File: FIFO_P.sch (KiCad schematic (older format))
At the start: 93 parts, among them J1 Vin, J2 ICLK, J3 Screw_Terminal_01x08, J4 Jack-DC, J5 Start Trigger, J6 Vout, SW1 Program History, SW2 Rotary_Encoder_61C, U1 IDT_ICS551, U10 AD7840, U11 LM2776, U2 SN74LVC2G157_MUX_TI, U3 SN74LVC2G157_MUX_TI, U4 LTC1740, U5 LM2940CT-5.0, U6 LM1117-3.3, U7 ARDUINO_DUE_FIFO_P_COMMANDS, U8 IDT_72V2105, U9 Adafruit_128x32_OLED_I2C_1306

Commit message: Calculated optimum DAC0 to ADC resistor values and fixed schematic
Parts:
- removed R?: 30R1, symbol Device:R
- removed R?: 10k, symbol Device:R
- removed R?: 220R, symbol Device:R
- added R?: 30R1, symbol Device:R
- R?: value 220R -> 1k1
- R? (x3): value 10k -> 5k1
- R?: value 10k -> 4k3
- R?: value 10k -> 1k1
- R?: value 10k -> 3k9
- RV?: value 5k -> 1k
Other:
- moved on the sheet: C?, R?, RV?, U?, U?A, U?B, U?C

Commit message: Updated schematic for dual clock operation; Squished everything!
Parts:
- removed C11: 1u, Capacitor_SMD:C_0805_2012Metric_Pad1.15x1.40mm_HandSolder, symbol Device:C
- removed C8: 0u1, Capacitor_SMD:C_0805_2012Metric_Pad1.15x1.40mm_HandSolder, symbol Device:C
- removed J2: ICLK, Connector_Coaxial:BNC_TEConnectivity_1478204_Vertical, symbol Connector:Conn_Coaxial
- removed R2: 49R9, Resistor_SMD:R_0805_2012Metric_Pad1.15x1.40mm_HandSolder, symbol Device:R
- removed SW1: Program History, Button_Switch_THT:SW_Slide_1P2T_CK_OS102011MS2Q, symbol Switch:SW_SPDT
- removed TP2: TestPoint, FIFO_P:Test_Pin, symbol Connector:TestPoint
- removed U1: IDT_ICS551, Package_SO:SOIC-8_3.9x4.9mm_P1.27mm, symbol FIFO_P:IDT_ICS551
- added C12: 1u, Capacitor_SMD:C_0805_2012Metric_Pad1.15x1.40mm_HandSolder, symbol Device:C
- added C20, C21, C9: 0u1, Capacitor_SMD:C_0805_2012Metric_Pad1.15x1.40mm_HandSolder, symbol Device:C
- added C42, C43: 10u, Capacitor_SMD:C_0805_2012Metric_Pad1.15x1.40mm_HandSolder, symbol Device:C
- added J4: XWCLK, Connector_Coaxial:BNC_TEConnectivity_1478204_Vertical, symbol Connector:Conn_Coaxial
- added J5: XRCLK, Connector_Coaxial:BNC_TEConnectivity_1478204_Vertical, symbol Connector:Conn_Coaxial
- added R7, R8: 49R9, Resistor_SMD:R_0805_2012Metric_Pad1.15x1.40mm_HandSolder, symbol Device:R
- added U2: SN74LVC2G157_MUX_TI, Package_SO:SSOP-8_2.95x2.8mm_P0.65mm, symbol FIFO_P:SN74LVC2G157_MUX_TI
- added U3: TS12A12511, Package_TO_SOT_SMD:SOT-23-8_Handsoldering, symbol FIFO_P:TS12A12511
- C13, C44: renamed from C?; footprint (none) -> Capacitor_SMD:C_0805_2012Metric_Pad1.15x1.40mm_HandSolder
- R10: renamed from R7; footprint Resistor_THT:R_Axial_DIN0207_L6.3mm_D2.5mm_P10.16mm_Horizontal -> Resistor_SMD:R_0805_2012Metric_Pad1.15x1.40mm_HandSolder
- R11, R14, R15, R16, R17, R18, R5, R9: renamed from R?; footprint (none) -> Resistor_SMD:R_0805_2012Metric_Pad1.15x1.40mm_HandSolder
- R12: renamed from R8; footprint Resistor_THT:R_Axial_DIN0207_L6.3mm_D2.5mm_P10.16mm_Horizontal -> Resistor_SMD:R_0805_2012Metric_Pad1.15x1.40mm_HandSolder
- R13: renamed from R9; footprint Resistor_THT:R_Axial_DIN0207_L6.3mm_D2.5mm_P10.16mm_Horizontal -> Resistor_SMD:R_0805_2012Metric_Pad1.15x1.40mm_HandSolder
- R3: value 30R1 -> 22R6
- R6: footprint Resistor_THT:R_Axial_DIN0204_L3.6mm_D1.6mm_P7.62mm_Horizontal -> Resistor_SMD:R_0805_2012Metric_Pad1.15x1.40mm_HandSolder
- RV1, RV3: renamed from RV?; footprint (none) -> Potentiometer_SMD:Potentiometer_Vishay_TS53YL_Vertical
- SW1: renamed from SW2; footprint Connector_PinHeader_2.54mm:PinHeader_1x06_P2.54mm_Vertical -> FIFO_P:Rotary_Encoder_61C
- U10: renamed from U9; footprint Connector_PinHeader_2.54mm:PinHeader_1x06_P2.54mm_Vertical -> FIFO_P:Adafruit_128x32_OLED_I2C_1306
- U12: renamed from U?; footprint Package_TO_SOT_THT:TO-92_Inline -> Package_TO_SOT_SMD:SOT-23_Handsoldering
- U14: renamed from U?; footprint (none) -> Package_SO:SOIC-8_3.9x4.9mm_P1.27mm
- renumbered C12 to C11, C13 to C14, C14 to C15, C15 to C16, C16 to C17, C17 to C18, C18 to C19, C19 to C22, C20 to C23, C21 to C24, C22 to C25, C23 to C26, C24 to C27, C25 to C28, C26 to C29, C27 to C30, C28 to C31, C29 to C32, C30 to C33, C31 to C34, C32 to C35, C33 to C36, C36 to C37, C34 to C38, C35 to C39, C37 to C40, C38 to C41, C9 to C8, J3 to J2, J4 to J3, J5 to J6, J6 to J7, R4 to R2, R5 to R4, RV1 to RV2, TP3 to TP2, TP4 to TP3, TP5 to TP4, TP6 to TP5, TP7 to TP6, U2 to U1, U10 to U11, U11 to U13, U3 to U4, U4 to U5, U5 to U6, U6 to U7, U7 to U8, U8 to U9
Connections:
- net labels added: ADC_CLK_S, PROG_D, RHALT
- net labels removed: DAC_WR, WLSTN
- wire segments 443 -> 456
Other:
- note added: "TS12A12511 Decoupling"
- note removed: "Analog star\nGND"
- moved on the sheet: C10, C11, C13, C14, C33, C34, C35, C36, C37, C38, C39, C40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

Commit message: Fixed Due power and added AND gate for FIFO ~RE
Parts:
- added U11: 74AHC1G08, Package_SO:TSOP-5_1.65x3.05mm_P0.95mm, symbol 74xGxx:74AHC1G08
- renumbered R9 to R10, R12 to R11, R13 to R12, R11 to R13, R10 to R9, U11 to U12, U12 to U13, U13 to U14, U14 to U15
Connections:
- net labels added: A1, A2, RST1
- wire segments 456 -> 459
- no-connect marks 12 -> 9
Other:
- moved on the sheet: U10

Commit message: Almost done routing!
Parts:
- removed R2, R3, R4: 22R6, Resistor_SMD:R_0805_2012Metric_Pad1.15x1.40mm_HandSolder, symbol Device:R
- renumbered C14 to C13, C15 to C14, C16 to C15, C17 to C16, C18 to C17, C19 to C18, C20 to C19, C21 to C20, C22 to C21, C23 to C22, C24 to C23, C25 to C24, C26 to C25, C27 to C26, C28 to C27, C29 to C28, C30 to C29, C31 to C30, C32 to C31, C13 to C32, R13 to R10, R14 to R11, R15 to R12, R16 to R13, R17 to R14, R18 to R15, R6 to R2, R7 to R3, R8 to R4, R9 to R6, R10 to R7, R11 to R8, R12 to R9, U3 to U1, U1 to U2, U2 to U3
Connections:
- net labels added: ~PROG
- wire segments 459 -> 458
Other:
- note added: "MUX out Z: about 22R6"
- moved on the sheet: C32, R5, U1

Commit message: Done with main circuit. TODO: EXT header and input protection
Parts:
- removed TP1, TP2, TP3, TP4, TP5, TP6: TestPoint, FIFO_P:Test_Pin, symbol Connector:TestPoint
- added J6: Conn_02x04_Odd_Even, Connector_PinSocket_2.54mm:PinSocket_2x04_P2.54mm_Vertical, symbol Connector_Generic:Conn_02x04_Odd_Even
- added R2: 22R, Resistor_SMD:R_0805_2012Metric_Pad1.15x1.40mm_HandSolder, symbol Device:R
- R10: renamed from R9; value 10k -> 5k1
- R6: renamed from R5; value 30R1 -> 22R
- R7: renamed from R6; value 3k3 -> 5k1
- R9: renamed from R8; value 3k3 -> 5k1
- renumbered J6 to J7, J7 to J8, R10 to R11, R11 to R12, R12 to R13, R13 to R14, R14 to R15, R15 to R16, R2 to R3, R3 to R4, R4 to R5, R7 to R8
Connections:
- net labels removed: CLK_EN, PROG, RCLK_S, RLSTN
- wire segments 458 -> 467
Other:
- note removed: "MUX out Z: about 22R6"
- moved on the sheet: J7

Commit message: Board pretty much done. Cleaned up silkscreen
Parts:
- added Q1: DMP3099L, Package_TO_SOT_SMD:SOT-23, symbol FIFO_P:DMP3099L
- added TP1: GND, FIFO_P:Test_Pin, symbol Connector:TestPoint_Alt
- added TP2: +5V, FIFO_P:Test_Pin, symbol Connector:TestPoint_Alt
- added TP3: -5V, FIFO_P:Test_Pin, symbol Connector:TestPoint_Alt
- added TP4: 3.3V, FIFO_P:Test_Pin, symbol Connector:TestPoint_Alt
- renumbered C17 to C16, C18 to C17, C19 to C18, C16 to C19, C23 to C22, C22 to C23, C6 to C5, C5 to C6, C8 to C7, C9 to C8, C7 to C9, J3 to J2, J2 to J3
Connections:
- net +5V: now also TP2.1
- net -5V: now also TP3.1
- net A1: now also U8.A1
- net A2: now also U8.A2
- net GND: now also Q1.1 (G), TP1.1
- net RST1: now also U8.RST1
- net V+: now also Q1.2 (S); no longer J2.1, J3.8 (Pin_8)
- net VCC: now also TP4.1
- net at U8.5V3 (EXT_5V): now also J6.2 (Pin_2)
- net at U8.D23: now also J6.6 (Pin_6); no longer J6.5 (Pin_5)
- net at U8.D25: now also J6.8 (Pin_8); no longer J6.7 (Pin_7)
- net at U8.D27: now also J6.7 (Pin_7); no longer J6.8 (Pin_8)
- net at U8.D29: now also J6.5 (Pin_5); no longer J6.6 (Pin_6)
- new net: J2.1, J3.8 (Pin_8), Q1.3 (D)
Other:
- note added: "Reverse\nVoltage\nProtection"
- moved on the sheet: C14, C15, C19, C23, C24, C25, C4, C6, C9, J2, J6, U6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

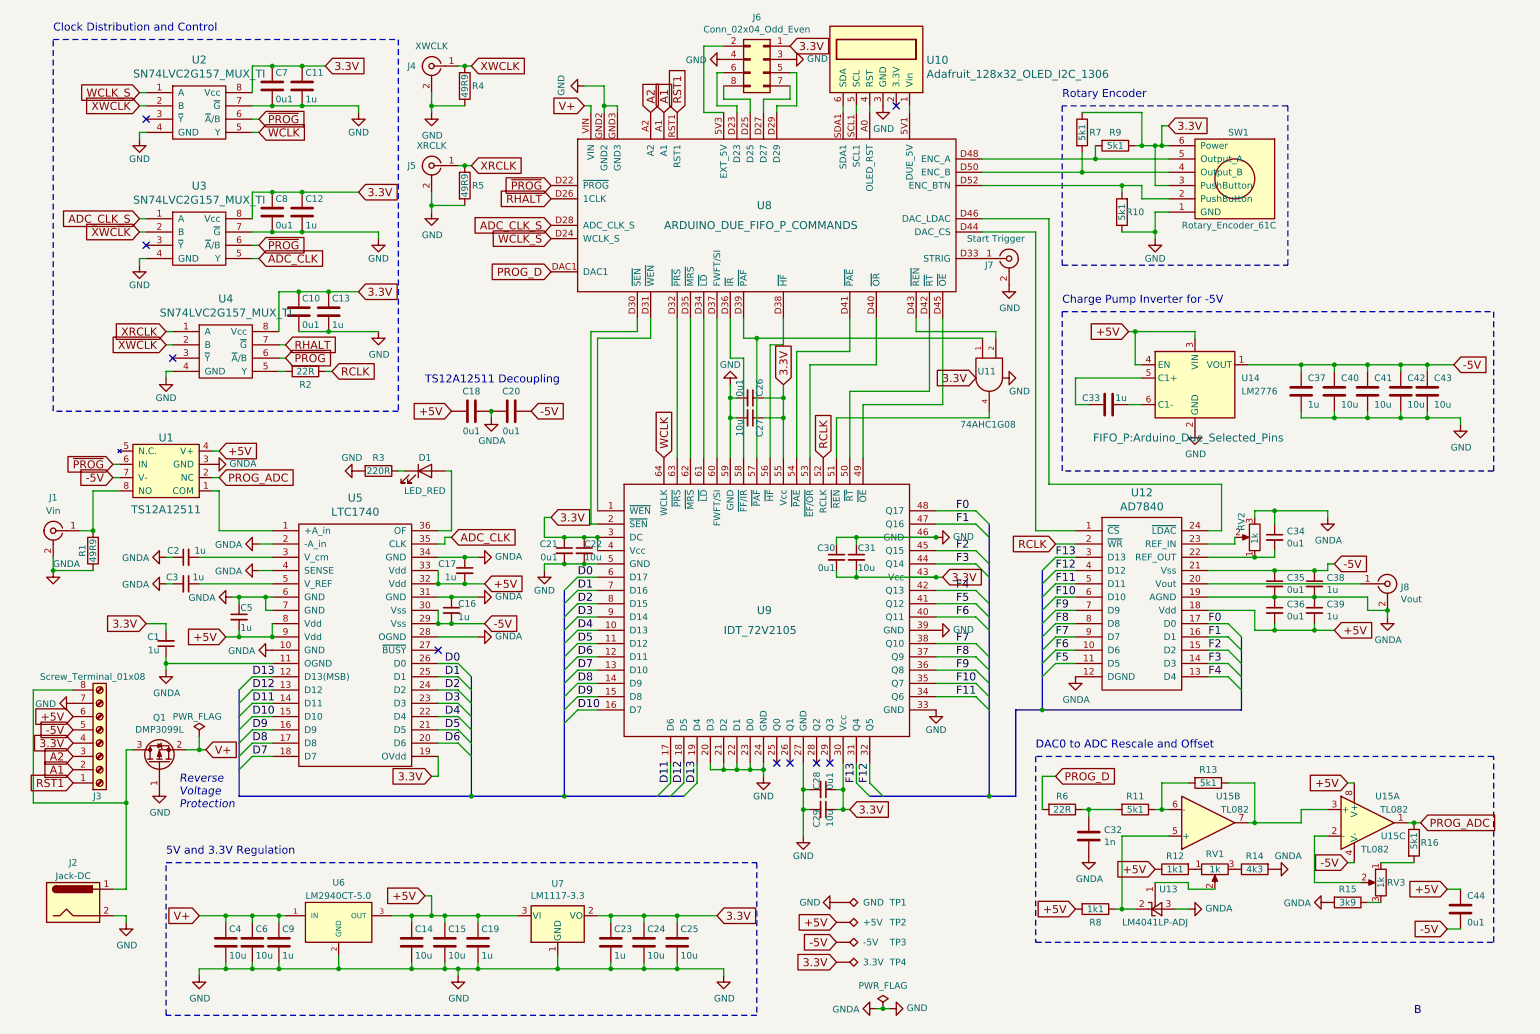
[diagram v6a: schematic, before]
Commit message: Fixed 1CLK signal. Board complete.
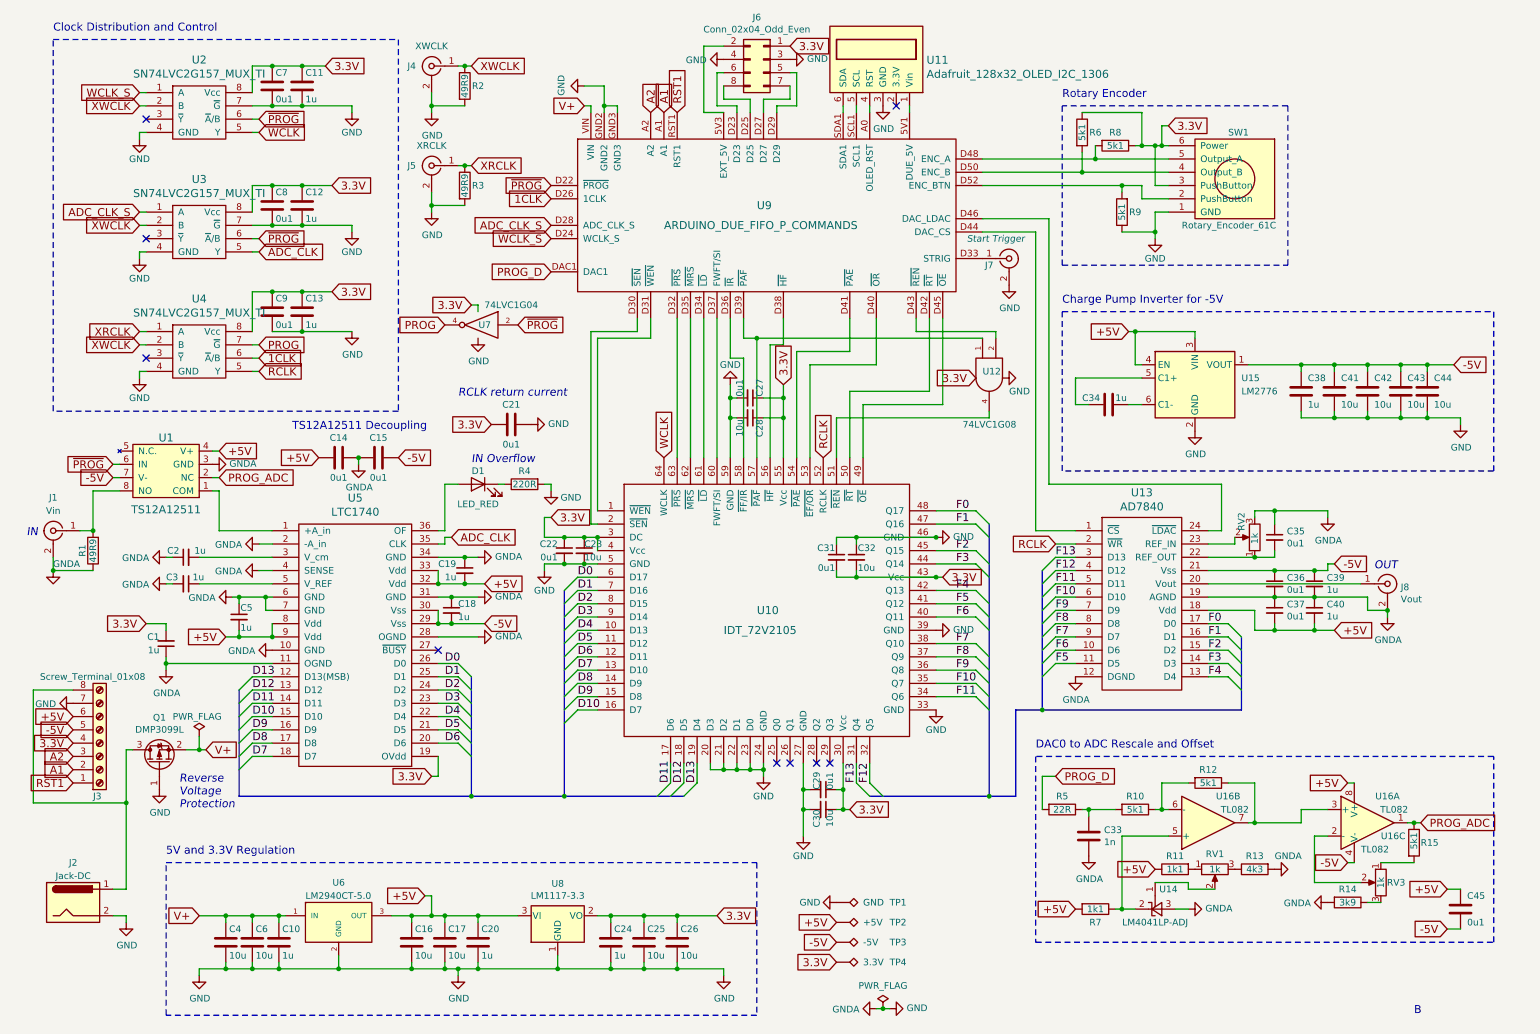
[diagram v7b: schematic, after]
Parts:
- removed R2: 22R, Resistor_SMD:R_0805_2012Metric_Pad1.15x1.40mm_HandSolder, symbol Device:R
- removed U11: 74AHC1G08, Package_SO:TSOP-5_1.65x3.05mm_P0.95mm, symbol 74xGxx:74AHC1G08
- added C21: 0u1, Capacitor_SMD:C_0805_2012Metric_Pad1.15x1.40mm_HandSolder, symbol Device:C
- added U12: 74LVC1G08, Package_TO_SOT_SMD:SOT-23-5_HandSoldering, symbol 74xGxx:74LVC1G08
- added U7: 74LVC1G04, Package_TO_SOT_SMD:SOT-23-5_HandSoldering, symbol 74xGxx:74LVC1G04
- renumbered C9 to C10, C18 to C14, C20 to C15, C14 to C16, C15 to C17, C16 to C18, C17 to C19, C19 to C20, C21 to C22, C22 to C23, C23 to C24, C24 to C25, C25 to C26, C26 to C27, C27 to C28, C28 to C29, C29 to C30, C30 to C31, C31 to C32, C32 to C33, C33 to C34, C34 to C35, C35 to C36, C36 to C37, C37 to C38, C38 to C39, C39 to C40, C40 to C41, C41 to C42, C42 to C43, C43 to C44, C44 to C45, C10 to C9, R11 to R10, R12 to R11, R13 to R12, R14 to R13, R15 to R14, R16 to R15, R4 to R2, R5 to R3, R3 to R4, R6 to R5, R7 to R6, R8 to R7, R9 to R8, R10 to R9, U9 to U10, U10 to U11, U12 to U13, U13 to U14, U14 to U15, U15 to U16, U7 to U8, U8 to U9
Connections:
- net GND: now also C21.2, U12.3 (GND), U7.3 (GND)
- net RCLK: now also U4.5 (Y)
- net VCC: now also C21.1, U12.5 (VCC), U7.5 (VCC)
- net ~PROG: now also U7.2; no longer U4.6 (~A~/B~)
- net at U10.51 (~REN): now also U12.4
- net at U10.57 (~PAF), U9.D39 (~PAF): now also U12.1
- net at U9.D43 (~REN): now also U12.2
- net RHALT renamed 1CLK
- net 1CLK: now also U4.6 (~A~/B~); no longer U4.7 (~G)
- new net PROG: U4.7 (~G), U7.4
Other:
- note added: "IN"
- note added: "IN Overflow"
- note added: "OUT"
- note added: "RCLK return current"
- moved on the sheet: C12, C13, C14, C15, C8, C9, D1, R4, U3, U4

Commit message: Moved power connector for new Due header clearance
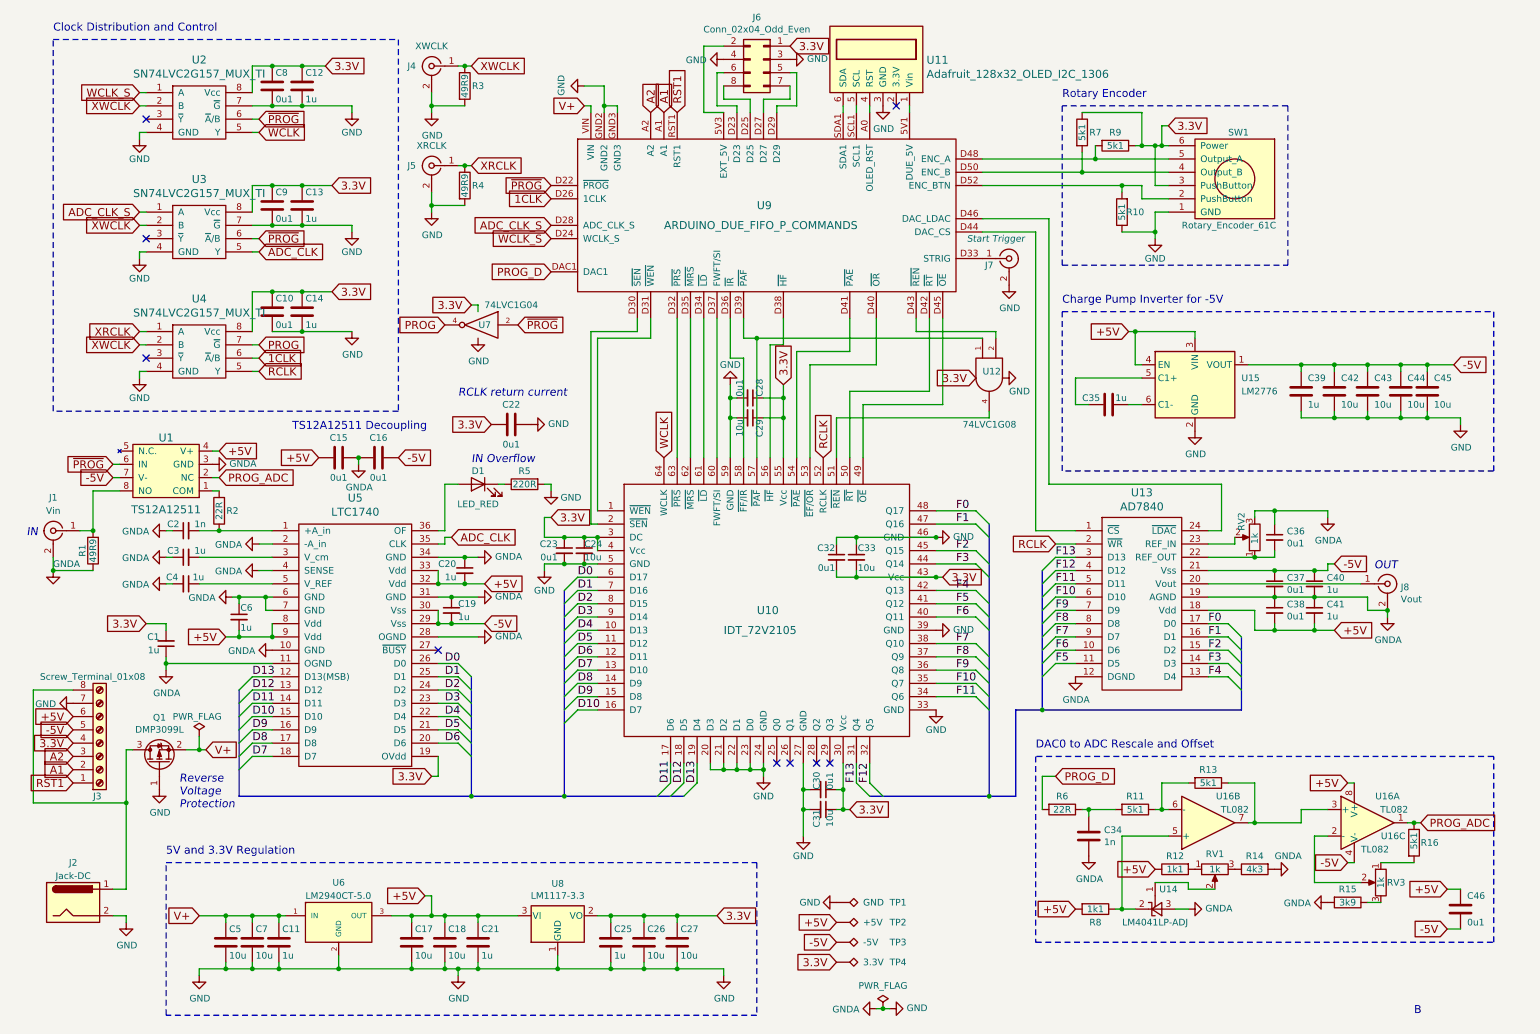
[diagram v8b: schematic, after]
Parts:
- added C2: 1n, Capacitor_SMD:C_0805_2012Metric_Pad1.15x1.40mm_HandSolder, symbol Device:C_Small
- added R2: 22R, Resistor_SMD:R_0805_2012Metric_Pad1.15x1.40mm_HandSolder, symbol Device:R
- renumbered C9 to C10, C10 to C11, C11 to C12, C12 to C13, C13 to C14, C14 to C15, C15 to C16, C16 to C17, C17 to C18, C18 to C19, C19 to C20, C20 to C21, C21 to C22, C22 to C23, C23 to C24, C24 to C25, C25 to C26, C26 to C27, C27 to C28, C28 to C29, C2 to C3, C29 to C30, C30 to C31, C31 to C32, C32 to C33, C33 to C34, C34 to C35, C35 to C36, C36 to C37, C37 to C38, C38 to C39, C3 to C4, C39 to C40, C40 to C41, C41 to C42, C42 to C43, C43 to C44, C44 to C45, C45 to C46, C4 to C5, C5 to C6, C6 to C7, C7 to C8, C8 to C9, R9 to R10, R10 to R11, R11 to R12, R12 to R13, R13 to R14, R14 to R15, R15 to R16, R2 to R3, R3 to R4, R4 to R5, R5 to R6, R6 to R7, R7 to R8, R8 to R9
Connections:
- net GND: now also C2.1
- net at U5.1 (+A_in): now also C2.2, R2.1; no longer U1.1 (COM)
- new net: R2.2, U1.1 (COM)
